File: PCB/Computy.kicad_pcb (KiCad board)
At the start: 2 copper layers, 50 x 100 mm, 47 parts, among them J1 USB_C_Receptacle_USB2.0_16P, J2 Conn_ARM_JTAG_SWD_10, J3 Conn_01x03_Socket, J4 Conn_01x04_Socket, J5 Conn_02x04_Odd_Even, M1 Motor_Servo, M2 Motor_Servo, M3 Motor_Servo, M4 Motor_Servo, M5 Motor_Servo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

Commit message: Minor PCB changes
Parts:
- moved C2 0.50 mm to (115.5, 104.5)
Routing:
- net GND: track 92.0 -> 92.8 mm
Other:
- board text added: "NRST"
- board text added: "SWCLK"
- board text added: "SWDIO"
- board text added: "SWO"

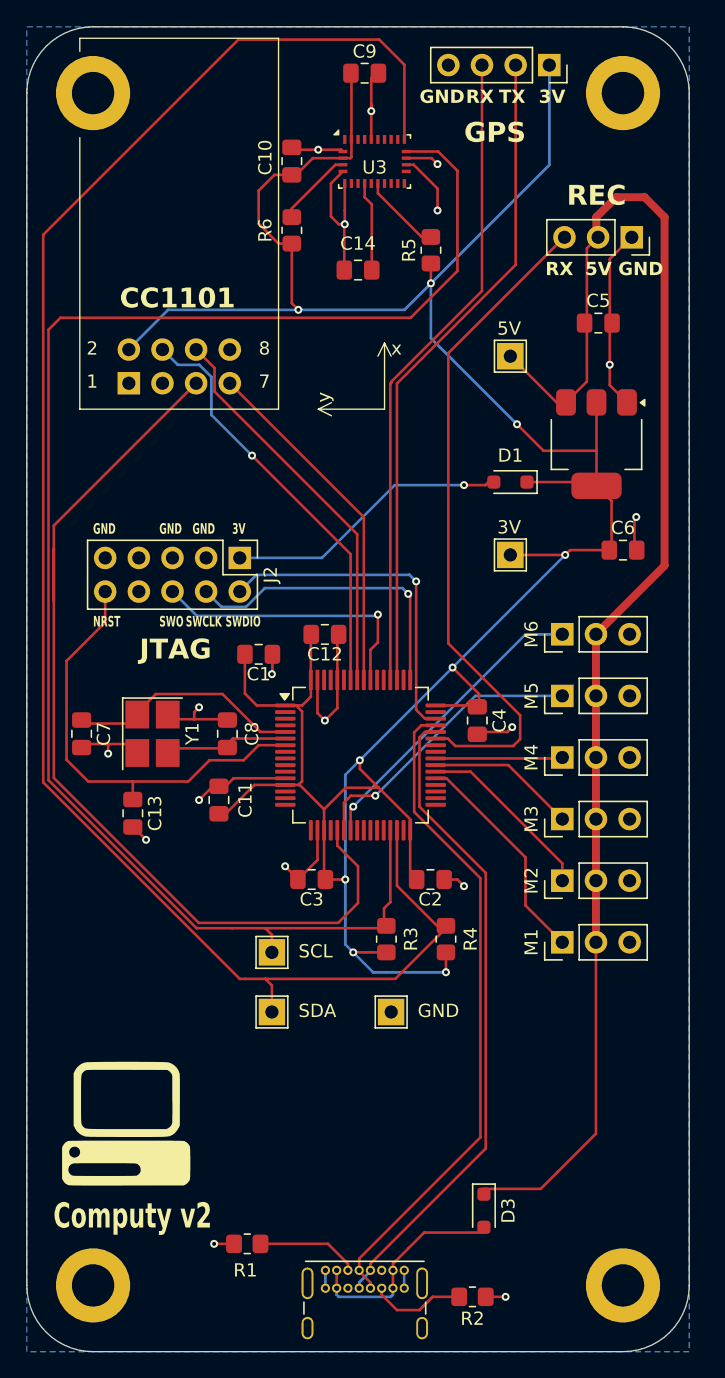
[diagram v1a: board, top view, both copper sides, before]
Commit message: Add DF13 connector for GPS and telemetry
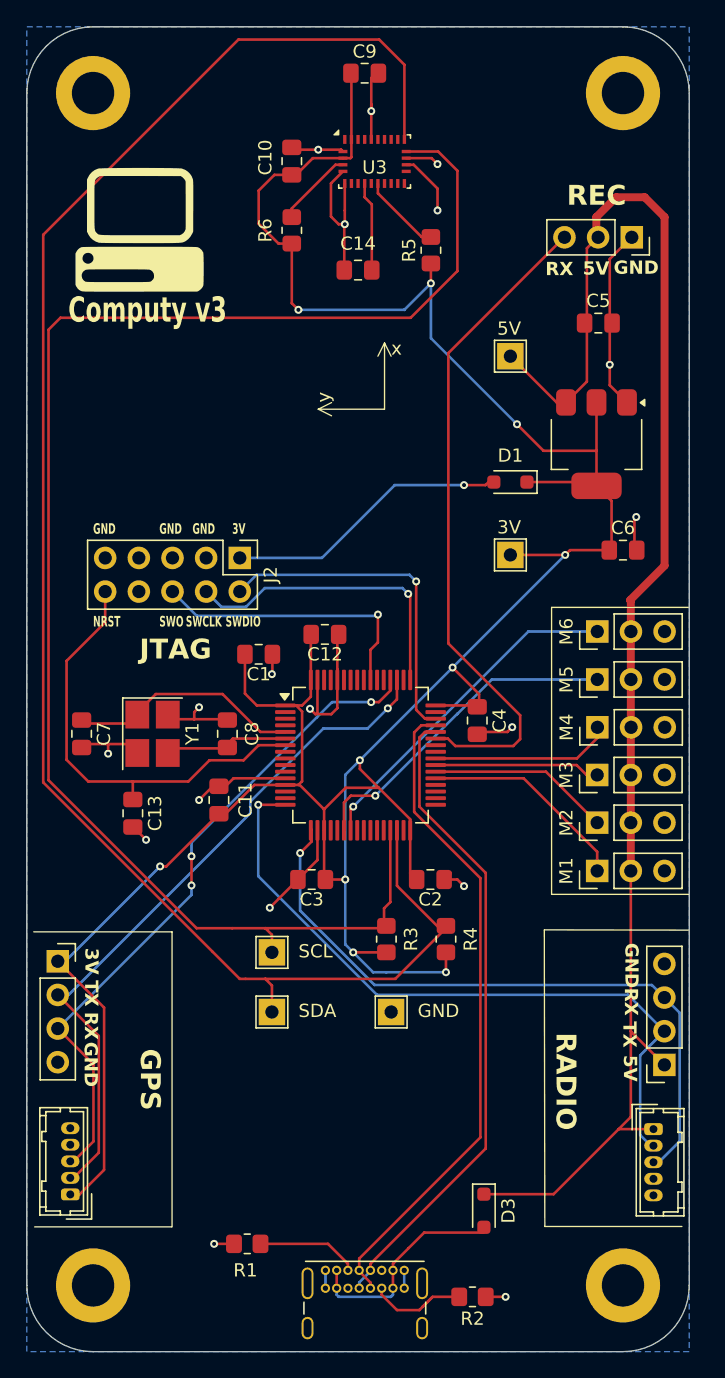
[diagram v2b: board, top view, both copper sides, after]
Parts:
- added J6: Conn_01x05, Connector_Hirose:Hirose_DF13-05P-1.25DSA_1x05_P1.25mm_Vertical, F.Cu at (132.3, 123.3)
- added J7: Conn_01x05, Connector_Hirose:Hirose_DF13-05P-1.25DSA_1x05_P1.25mm_Vertical, F.Cu at (88.3, 128.3)
- J5: value Conn_02x04_Odd_Even -> Conn_01x04_Socket; footprint Connector_PinSocket_2.54mm:PinSocket_2x04_P2.54mm_Vertical -> Connector_PinSocket_2.54mm:PinSocket_1x04_P2.54mm_Vertical; moved to F.Cu
- moved J4 77.2 mm to (87.3, 110.7), turned to 0 degrees
- moved G*** 67.5 mm to (93.5, 55.5)
- moved J5 65.4 mm to (133.1, 118.5), turned to 180 degrees
- moved M1 6.00 mm to (128.1, 103.8)
- moved M2 5.11 mm to (128.1, 100.2)
- moved M3 4.24 mm to (128.1, 96.6)
- moved M4 3.49 mm to (128.1, 93.0)
- moved M5 2.92 mm to (128.1, 89.4)
- moved M6 2.65 mm to (128.1, 85.8)
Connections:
- H1 pad 1: GND -> (no net)
- H2 pad 1: GND -> (no net)
- H3 pad 1: GND -> (no net)
- H4 pad 1: GND -> (no net)
- J5 pad 1: GND -> +5V
- J5 pad 2: +3.3V -> /RADIO_TX
- J5 pad 3: unconnected-(J5-Pin_3-Pad3) -> /RADIO_RX
- J5 pad 4: /CC1101_CSN -> GND
- U1 pad 16: unconnected-(U1-PA2-Pad16) -> /RADIO_TX
- U1 pad 17: unconnected-(U1-PA3-Pad17) -> /RADIO_RX
- U1 pad 21: /SPI1_SCK -> unconnected-(U1-PA5-Pad21)
- U1 pad 56: /SPI1_MISO -> unconnected-(U1-PB4-Pad56)
- U1 pad 57: /SPI1_MOSI -> unconnected-(U1-PB5-Pad57)
- U1 pad 58: /CC1101_CSN -> unconnected-(U1-PB6-Pad58)
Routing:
- net /SPI1_SCK: track 72.5 -> 0.00 mm
- net /RADIO_TX: track 0.00 -> 52.9 mm, vias 0 -> 1
- net /RADIO_RX: track 0.00 -> 51.1 mm, vias 0 -> 1
- net /CC1101_CSN: track 31.8 -> 0.00 mm, vias 1 -> 0
- net /SPI1_MOSI: track 30.0 -> 0.00 mm
- net /SPI1_MISO: track 26.6 -> 0.00 mm
- net +5V: track 108.6 -> 115.8 mm
- net /TIM8_CH4: track 9.59 -> 13.6 mm
- net /TIM3_CH1: track 21.9 -> 25.1 mm
- net +3.3V: track 224.0 -> 227.1 mm, vias 9 -> 10
- net TX_GPS: track 50.1 -> 53.1 mm, vias 0 -> 1
- net /TIM3_CH2: track 23.0 -> 25.8 mm
- net GND: track 92.8 -> 94.8 mm
- net RX_GPS: track 49.3 -> 50.8 mm, vias 0 -> 3
- net /TIM8_CH3: track 11.2 -> 12.5 mm
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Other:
- board text added: "Computy v3"
- board text added: "RADIO"
- board text removed: "1"
- board text removed: "2"
- board text removed: "7"
- board text removed: "8"
- board text removed: "CC1101"
- board text removed: "Computy v2"

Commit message: Add CAN transceiver
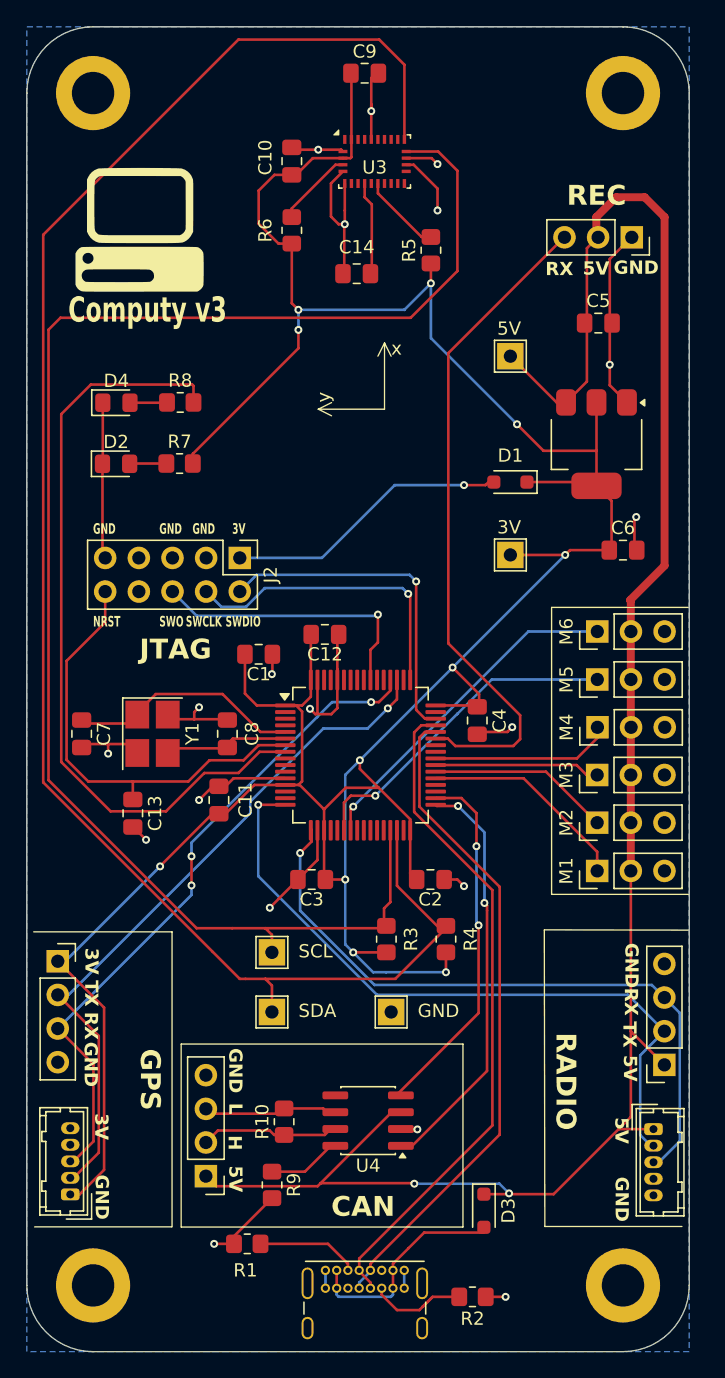
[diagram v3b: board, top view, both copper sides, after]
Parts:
- added D2: LED, LED_SMD:LED_0805_2012Metric_Pad1.15x1.40mm_HandSolder, F.Cu at (91.7, 73.1)
- added D4: LED, LED_SMD:LED_0805_2012Metric_Pad1.15x1.40mm_HandSolder, F.Cu at (91.8, 68.5)
- added J8: Conn_01x04_Socket, Connector_PinHeader_2.54mm:PinHeader_1x04_P2.54mm_Vertical, F.Cu at (98.5, 126.9)
- added R10: 120, Resistor_SMD:R_0805_2012Metric_Pad1.20x1.40mm_HandSolder, F.Cu at (104.4, 122.8)
- added R7: 220, Resistor_SMD:R_0805_2012Metric_Pad1.20x1.40mm_HandSolder, F.Cu at (96.5, 73.1)
- added R8: 220, Resistor_SMD:R_0805_2012Metric_Pad1.20x1.40mm_HandSolder, F.Cu at (96.6, 68.5)
- added R9: 10k, Resistor_SMD:R_0805_2012Metric_Pad1.20x1.40mm_HandSolder, F.Cu at (103.5, 127.5)
- added U4: MCP2558FD-xSN, Package_SO:SOIC-8_3.9x4.9mm_P1.27mm, F.Cu at (110.8, 122.7)
- moved C14 0.29 mm to (109.9, 58.8)
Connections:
- U1 pad 33: unconnected-(U1-PB12-Pad33) -> /CAN2_TX
- U1 pad 34: unconnected-(U1-PB13-Pad34) -> /CAN2_RX
- U1 pad 8: unconnected-(U1-PC0-Pad8) -> /LED_MCU
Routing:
- net /LED_MCU: track 0.00 -> 58.8 mm
- net /CAN2_TX: track 0.00 -> 32.0 mm, vias 0 -> 2
- net +5V: track 115.8 -> 147.1 mm, vias 0 -> 2
- net /CAN2_RX: track 0.00 -> 27.8 mm, vias 0 -> 2
- net GND: track 94.8 -> 113.1 mm, vias 18 -> 19
- net +3.3V: track 227.1 -> 242.1 mm, vias 10 -> 11
- net /CAN_H: track 0.00 -> 9.92 mm
- net /CAN_L: track 0.00 -> 9.77 mm
- net Net-(U4-S): track 0.00 -> 5.03 mm
- net Net-(D4-A): track 0.00 -> 2.80 mm
- net Net-(D2-A): track 0.00 -> 2.78 mm
- net /USB_D-: track 49.0 -> 49.9 mm
- net /USB_D+: track 50.0 -> 50.8 mm
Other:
- board text added: "CAN"
- board text added: "H"
- board text added: "L"

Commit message: Minor changes
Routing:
- net GND: track 113.1 -> 114.8 mm
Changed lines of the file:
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@@
-	)
-	(segment
-		(start 114.365 123.475)
-		(end 114.48 123.36)
-		(width 0.2)
-		(layer "F.Cu")
-		(net 2)
 	)
 	(segment
@@
 	)
 	(segment
-		(start 112.745 123.475)
-		(end 114.365 123.475)
-		(width 0.2)
-		(layer "F.Cu")
-		(net 2)
-	)
-	(segment
 		(start 106.9375 103.025)
 		(end 105.4625 104.5)
@@
 	)
 	(segment
+		(start 114.365 123.475)
+		(end 112.745 123.475)
+		(width 0.2)
+		(layer "F.Cu")
+		(net 2)
+	)
+	(segment
 		(start 90.71 73.12)
 		(end 90.71 80.02)
@@
 	)
 	(segment
+		(start 115.56 122.09)
+		(end 115.56 122.28)
+		(width 0.2)
+		(layer "F.Cu")
+		(net 2)
+	)
+	(segment
 		(start 108.9625 55.075)
 		(end 108.9625 58.5)
@@
 		(start 121.6375 93)
 		(end 121.275 93.3625)
+		(width 0.2)
+		(layer "F.Cu")
+		(net 2)
+	)
+	(segment
+		(start 115.56 122.28)
+		(end 114.365 123.475)
 		(width 0.2)
 		(layer "F.Cu")
@@
 	)
 	(via
-		(at 114.48 123.36)
+		(at 115.56 122.09)
 		(size 0.6)
 		(drill 0.3)

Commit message: PCB fixes
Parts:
- added C15: 100nF, Capacitor_SMD:C_0805_2012Metric_Pad1.18x1.45mm_HandSolder, F.Cu at (116.7, 118.0)
- added C16: 100nF, Capacitor_SMD:C_0805_2012Metric_Pad1.18x1.45mm_HandSolder, F.Cu at (105.1, 118.0)
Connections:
- U1 pad 33: /CAN2_TX -> /CAN2_RX
- U1 pad 34: /CAN2_RX -> /CAN2_TX
- U4 pad 5: unconnected-(U4-VIO-Pad5) -> +3.3V
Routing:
- net +3.3V: track 242.1 -> 259.9 mm
- net GND: track 114.8 -> 125.9 mm
- net +5V: track 147.1 -> 152.8 mm
- net /CAN2_RX: track 27.8 -> 31.1 mm
- net /CAN2_TX: track 32.0 -> 33.1 mm

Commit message: Minor layout changes
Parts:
- moved C15 0.62 mm to (116.1, 118.0)
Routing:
- net /SWDIO: track 25.5 -> 21.3 mm, vias 1 -> 0
- net /CAN2_RX: track 31.1 -> 27.0 mm
- net /SWCLK: track 23.1 -> 19.3 mm, vias 1 -> 0
- net /SWO: track 21.5 -> 19.7 mm, vias 1 -> 0
- net +5V: track 152.8 -> 152.2 mm
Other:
- board text added: "RECEIVER"
- board text removed: "REC"
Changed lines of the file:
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@@
 		(tags "LGA 28 5.2x3.8mm Pitch 0.5mm")
 		(property "Reference" "U3"
-			(at 0 0.45 0)
+			(at 0 -0.008 0)
 			(layer "F.SilkS")
 			(effects
@@
 	(footprint "Capacitor_SMD:C_0805_2012Metric_Pad1.18x1.45mm_HandSolder"
 		(layer "F.Cu")
-		(at 116.7 117.99)
+		(at 116.078 117.99)
 		(descr "Capacitor SMD 0805 (2012 Metric), square (rectangular) end terminal, IPC-7351 nominal with elongated pad for handsoldering. (Body size source: IPC-SM-782 page 76, https://www.pcb-3d.com/wordpress/wp-content/uploads/ipc-sm-782a_amendment_1_and_2.pdf, https://docs.google.com/spreadsheets/d/1BsfQQcO9C6DZCsRaXUlFlo91Tg2WpOkGARC1WS5S8t0/edit?usp=sharing), generated with kicad-footprint-generator")
 		(tags "capacitor handsolder")
@@
 		(layer "F.SilkS")
 	)
+	(gr_rect
+		(start 121.666 50.8)
+		(end 134.366 59.69)
+		(stroke
+			(width 0.1)
+			(type default)
+		)
+		(fill no)
+		(layer "F.SilkS")
+	)
 	(gr_line
 		(start 124.06 108.32)
@@
 		)
 	)
-	(gr_text "REC"
-		(at 125.75 53.75 0)
+	(gr_text "RECEIVER"
+		(at 122.682 53.75 0)
 		(layer "F.SilkS")
 		(effects
@@
 			(keep_text_aligned yes)
 		)
-		(gr_text "5.0000 mm"
+		(gr_text "5,0000 mm"
 			(at 132.5 32.35 0)
 			(layer "Dwgs.User")
@@
 			(keep_text_aligned yes)
 		)
-		(gr_text "50.0000 mm"
+		(gr_text "50,0000 mm"
 			(at 110 150.85 0)
 			(layer "Dwgs.User")
@@
 			(keep_text_aligned yes)
 		)
-		(gr_text "5.0000 mm"
+		(gr_text "5,0000 mm"
 			(at 153.35 42.6375 90)
 			(layer "Dwgs.User")
@@
 			(keep_text_aligned yes)
 		)
-		(gr_text "100.0000 mm"
+		(gr_text "100,0000 mm"
 			(at 69.350001 90.1375 90)
 			(layer "Dwgs.User")
@@
 			(keep_text_aligned yes)
 		)
-		(gr_text "40.0000 mm"
+		(gr_text "40,0000 mm"
 			(at 110 32.35 0)
 			(layer "Dwgs.User")
@@
 	)
 	(segment
+		(start 117.1155 117.99)
+		(end 117.1155 120.5345)
+		(width 0.2)
+		(layer "F.Cu")
+		(net 2)
+	)
+	(segment
 		(start 117.5 104.5)
 		(end 118 105)
@@
 	)
 	(segment
-		(start 117.7375 117.99)
-		(end 117.7375 119.9125)
-		(width 0.2)
-		(layer "F.Cu")
-		(net 2)
-	)
-	(segment
 		(start 129 62.6375)
 		(end 129 57.6625)
@@
 	)
 	(segment
+		(start 117.1155 120.5345)
+		(end 115.56 122.09)
+		(width 0.2)
+		(layer "F.Cu")
+		(net 2)
+	)
+	(segment
 		(start 114.204 50.55)
 		(end 116 52.346)
@@
 	)
 	(segment
-		(start 117.7375 119.9125)
-		(end 115.56 122.09)
-		(width 0.2)
-		(layer "F.Cu")
-		(net 2)
-	)
-	(segment
 		(start 91.1375 94.275)
 		(end 91.1375 95)
@@
 	)
 	(segment
-		(start 110.9375 87.1625)
-		(end 110.9375 89.435)
+		(start 95.995 83.549)
+		(end 95.995 82.765)
 		(width 0.2)
 		(layer "F.Cu")
@@
 	)
 	(segment
-		(start 111.5 86.6)
-		(end 110.9375 87.1625)
+		(start 110.9375 89.435)
+		(end 110.9375 86.80134)
 		(width 0.2)
 		(layer "F.Cu")
@@
 	)
 	(segment
-		(start 111.5 84.5)
-		(end 111.5 86.6)
+		(start 110.9375 86.80134)
+		(end 108.97216 84.836)
 		(width 0.2)
 		(layer "F.Cu")
 		(net 39)
 	)
-	(via
-		(at 111.5 84.5)
-		(size 0.6)
-		(drill 0.3)
-		(layers "F.Cu" "B.Cu")
-		(net 39)
-	)
-	(segment
-		(start 111.399 84.601)
-		(end 97.831 84.601)
-		(width 0.2)
-		(layer "B.Cu")
-		(net 39)
-	)
 	(segment
-		(start 97.831 84.601)
-		(end 95.995 82.765)
+		(start 108.97216 84.836)
+		(end 97.282 84.836)
 		(width 0.2)
-		(layer "B.Cu")
+		(layer "F.Cu")
 		(net 39)
 	)
 	(segment
-		(start 111.5 84.5)
-		(end 111.399 84.601)
+		(start 97.282 84.836)
+		(end 95.995 83.549)
 		(width 0.2)
-		(layer "B.Cu")
+		(layer "F.Cu")
 		(net 39)
 	)
@@
 	)
 	(segment
+		(start 113.581968 122.0625)
+		(end 113.235 122.0625)
+		(width 0.2)
+		(layer "F.Cu")
+		(net 49)
+	)
+	(segment
 		(start 127.275 56.8475)
 		(end 127.985 56.1375)
@@
 	)
 	(segment
+		(start 115.0405 120.603968)
+		(end 113.581968 122.0625)
+		(width 0.2)
+		(layer "F.Cu")
+		(net 49)
+	)
+	(segment
 		(start 114.211 127.421)
 		(end 114.25 127.46)
@@
 	)
 	(segment
-		(start 114.209999 122.0625)
-		(end 115.6625 120.609999)
-		(width 0.2)
-		(layer "F.Cu")
-		(net 49)
-	)
-	(segment
 		(start 130.59 103.85)
 		(end 130.59 115.955)
@@
 	)
 	(segment
-		(start 115.6625 120.609999)
-		(end 115.6625 117.99)
+		(start 115.0405 117.99)
+		(end 115.0405 120.603968)
 		(width 0.2)
 		(layer "F.Cu")
@@
 	)
 	(segment
-		(start 113.235 122.0625)
-		(end 114.209999 122.0625)
-		(width 0.2)
-		(layer "F.Cu")
-		(net 49)
-	)
-	(segment
 		(start 125.7 68.4875)
 		(end 125.7 68.4)
@@
 	(segment
 		(start 114.3875 91.69241)
-		(end 115.05509 92.36)
+		(end 114.3875 87.4044)
 		(width 0.2)
 		(layer "F.Cu")
@@
 	)
 	(segment
-		(start 114.3875 82)
-		(end 114.3875 91.69241)
+		(start 109.7481 82.765)
+		(end 101.075 82.765)
 		(width 0.2)
 		(layer "F.Cu")
@@
 	)
 	(segment
-		(start 115.05509 92.36)
-		(end 115.8625 92.36)
+		(start 114.3875 91.69241)
+		(end 115.05509 92.36)
 		(width 0.2)
 		(layer "F.Cu")
 		(net 50)
 	)
-	(via
-		(at 114.3875 82)
-		(size 0.6)
-		(drill 0.3)
-		(layers "F.Cu" "B.Cu")
-		(net 50)
-	)
-	(segment
-		(start 113.8875 81.5)
-		(end 102.34 81.5)
-		(width 0.2)
-		(layer "B.Cu")
-		(net 50)
-	)
 	(segment
-		(start 102.34 81.5)
-		(end 101.075 82.765)
+		(start 114.3875 87.4044)
+		(end 109.7481 82.765)
 		(width 0.2)
-		(layer "B.Cu")
+		(layer "F.Cu")
 		(net 50)
 	)
 	(segment
-		(start 114.3875 82)
-		(end 113.8875 81.5)
+		(start 115.05509 92.36)
+		(end 115.8625 92.36)
 		(width 0.2)
-		(layer "B.Cu")
+		(layer "F.Cu")
 		(net 50)
 	)
@@
 	)
 	(segment
-		(start 113.9375 83.0875)
-		(end 113.9375 89.435)
+		(start 100.205 84.435)
+		(end 98.535 82.765)
 		(width 0.2)
 		(layer "F.Cu")
@@
 	)
 	(segment
-		(start 113.7875 82.9375)
-		(end 113.9375 83.0875)
+		(start 113.9375 87.5215)
+		(end 110.851 84.435)
 		(width 0.2)
 		(layer "F.Cu")
 		(net 77)
 	)
-	(via
-		(at 113.7875 82.9375)
-		(size 0.6)
-		(drill 0.3)
-		(layers "F.Cu" "B.Cu")
-		(net 77)
-	)
-	(segment
-		(start 101.551346 83.915)
-		(end 99.685 83.915)
-		(width 0.2)
-		(layer "B.Cu")
-		(net 77)
-	)
-	(segment
-		(start 102.966346 82.5)
-		(end 101.551346 83.915)
-		(width 0.2)
-		(layer "B.Cu")
-		(net 77)
-	)
 	(segment
-		(start 113.7875 82.9375)
-		(end 113.35 82.5)
+		(start 110.851 84.435)
+		(end 100.205 84.435)
 		(width 0.2)
-		(layer "B.Cu")
-		(net 77)
-	)
-	(segment
-		(start 113.35 82.5)
-		(end 102.966346 82.5)
-		(width 0.2)
-		(layer "B.Cu")
+		(layer "F.Cu")
 		(net 77)
 	)
 	(segment
-		(start 99.685 83.915)
-		(end 98.535 82.765)
+		(start 113.9375 89.435)
+		(end 113.9375 87.5215)
 		(width 0.2)
-		(layer "B.Cu")
+		(layer "F.Cu")
 		(net 77)
 	)
@@
 		(width 0.2)
 		(layer "B.Cu")
-		(net 93)
-	)
-	(segment
-		(start 118.939 106.16)
-		(end 118.939 102.021)
-		(width 0.2)
-		(layer "B.Cu")
